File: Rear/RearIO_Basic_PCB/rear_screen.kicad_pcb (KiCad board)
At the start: 2 copper layers, 99.5 x 79.4 mm, 49 parts, among them J1 Conn_01x02_Pin, J13 USB_C_Receptacle_USB2.0, J2 Conn_01x02_Pin, J3 Conn_01x02_Pin, J4 Conn_01x02_Pin, J5 Conn_01x02_Pin, J6 Conn_01x02_Pin, J7 Conn_01x08_Socket, Q1 NTMFS4C03N-HXY, Q2 NTMFS4C03N-HXY, Q3 NTMFS4C03N-HXY, Q4 NTMFS4C03N-HXY, Q6 NTMFS4C03N-HXY, Q7 NTMFS4C03N-HXY, U1 MIC4426, U2 MIC4426, U3 AOZ1280CI

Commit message: wip
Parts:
- moved D4 2.80 mm to (141.2, 129.6)
- moved Q3 2.80 mm to (140.0, 122.5)
- moved Q4 2.80 mm to (130.4, 122.5)
- moved J4 2.80 mm to (137.7, 133.0)
- moved D3 2.10 mm to (115.6, 129.7)
- moved J3 2.10 mm to (112.2, 133.0)
- moved Q6 2.10 mm to (111.2, 121.2)
- moved Q2 1.28 mm to (157.0, 122.9)
- moved D2 1.28 mm to (90.1, 129.6)
- moved D5 1.28 mm to (166.8, 129.7)
- moved J2 1.28 mm to (86.8, 133.0)
- moved J5 1.28 mm to (162.7, 133.1)
- moved Q1 1.28 mm to (170.2, 122.9)
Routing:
- net Net-(Q6-G): track 36.2 -> 37.0 mm
- net Net-(Q1-G): track 66.2 -> 65.7 mm
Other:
- outline, holes or cut-outs redrawn
- board text added: "HP1"
- board text added: "HP2"
- board text added: "INPUT"
- board text added: "LP1"
- board text added: "LP2"
- board text added: "v0.2 09/23"
- board text removed: "v0.1a 08/23"

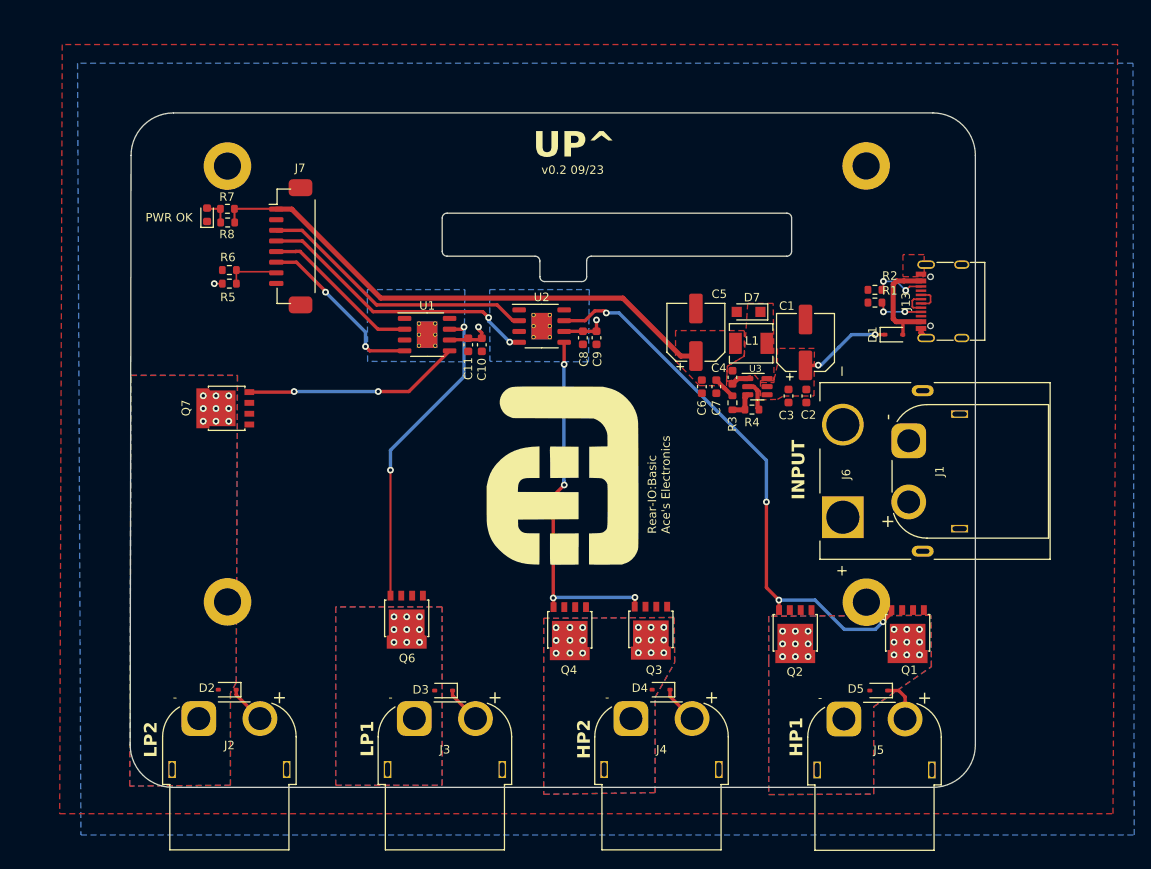
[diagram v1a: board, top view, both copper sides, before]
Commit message: small routing and layout changes, removed USB
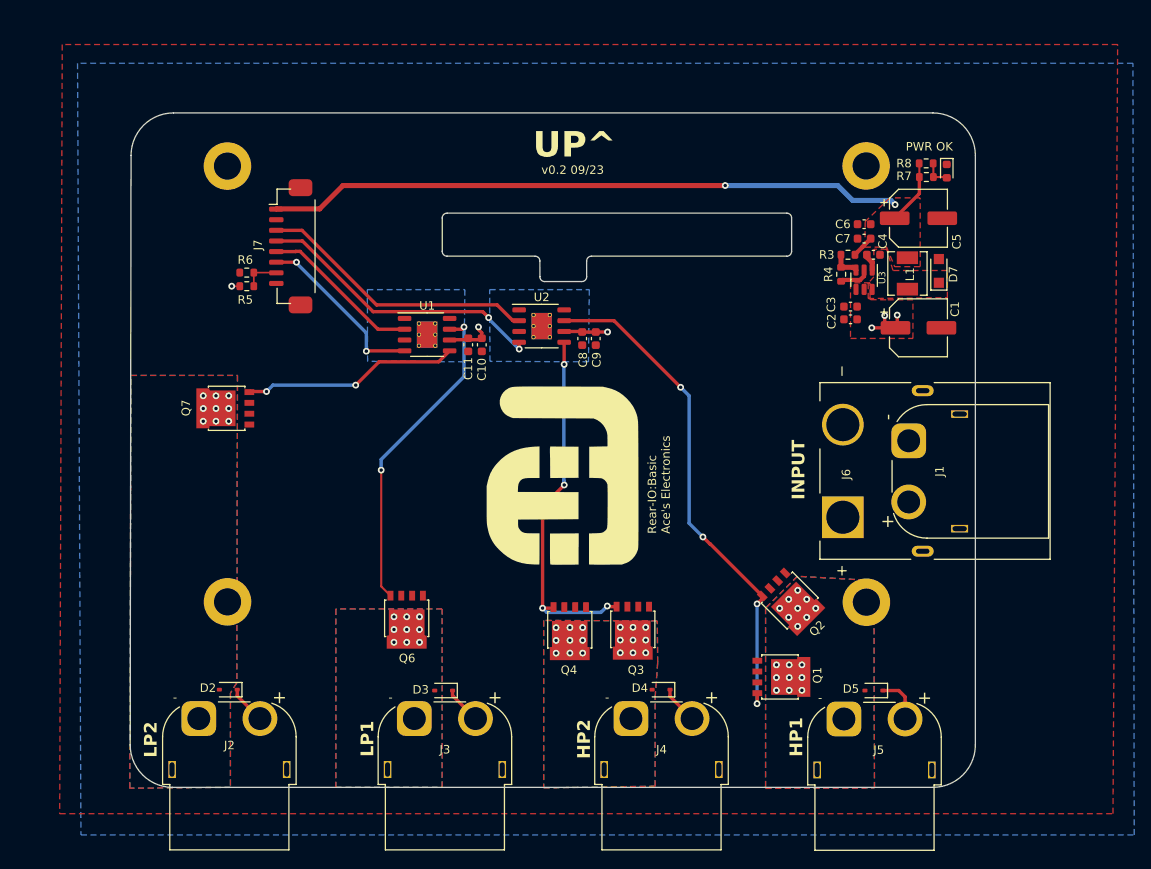
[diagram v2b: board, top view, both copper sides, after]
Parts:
- removed D1: 1N5819WS, Diode_SMD:D_SOD-323
- removed J13: USB_C_Receptacle_USB2.0, Connector_USB:USB_C_Receptacle_G-Switch_GT-USB-7010ASV
- removed R1, R2: 5.1k, Resistor_SMD:R_0603_1608Metric
- moved D6 87.2 mm to (174.8, 68.6), turned to -90 degrees
- moved R8 82.5 mm to (172.4, 67.6), turned to 0 degrees
- moved R7 82.4 mm to (172.4, 69.2), turned to 180 degrees
- moved C5 29.4 mm to (171.5, 74.1), turned to 0 degrees
- moved C6 27.0 mm to (165.1, 74.8), turned to 180 degrees
- moved C7 24.6 mm to (165.1, 76.5), turned to 180 degrees
- moved D7 22.9 mm to (173.9, 80.3), turned to 90 degrees
- moved R3 22.1 mm to (163.2, 78.4), turned to 180 degrees
- moved C4 22.0 mm to (166.2, 78.4), turned to 0 degrees
- moved L1 20.2 mm to (170.2, 80.6), turned to 90 degrees
- moved R4 19.1 mm to (162.4, 80.7), turned to -90 degrees
- moved U3 17.8 mm to (165.1, 81.3), turned to -90 degrees
- moved Q1 15.9 mm to (155.2, 128.1), turned to 0 degrees
- moved C1 13.4 mm to (171.5, 87.0), turned to 0 degrees
- moved C3 12.8 mm to (163.5, 84.5), turned to 180 degrees
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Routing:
- net +5V: track 65.8 -> 85.3 mm, vias 0 -> 2
- net VBUS: track 12.6 -> 0.00 mm
- net Net-(J13-CC2): track 6.14 -> 0.00 mm, vias 2 -> 0
- net Net-(Q1-G): track 65.7 -> 59.7 mm
- net Net-(J13-CC1): track 5.61 -> 0.00 mm, vias 2 -> 0
- net VIN: track 40.8 -> 37.0 mm, vias 5 -> 6
- net USB_D+: track 3.09 -> 0.00 mm
- net USB_D-: track 2.89 -> 0.00 mm
- net GPIO14: track 6.41 -> 4.21 mm
- net GND: track 5.03 -> 3.66 mm
- net GPIO11: track 33.8 -> 34.8 mm
- net Net-(Q6-G): track 37.0 -> 37.9 mm

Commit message: routing and layout changes
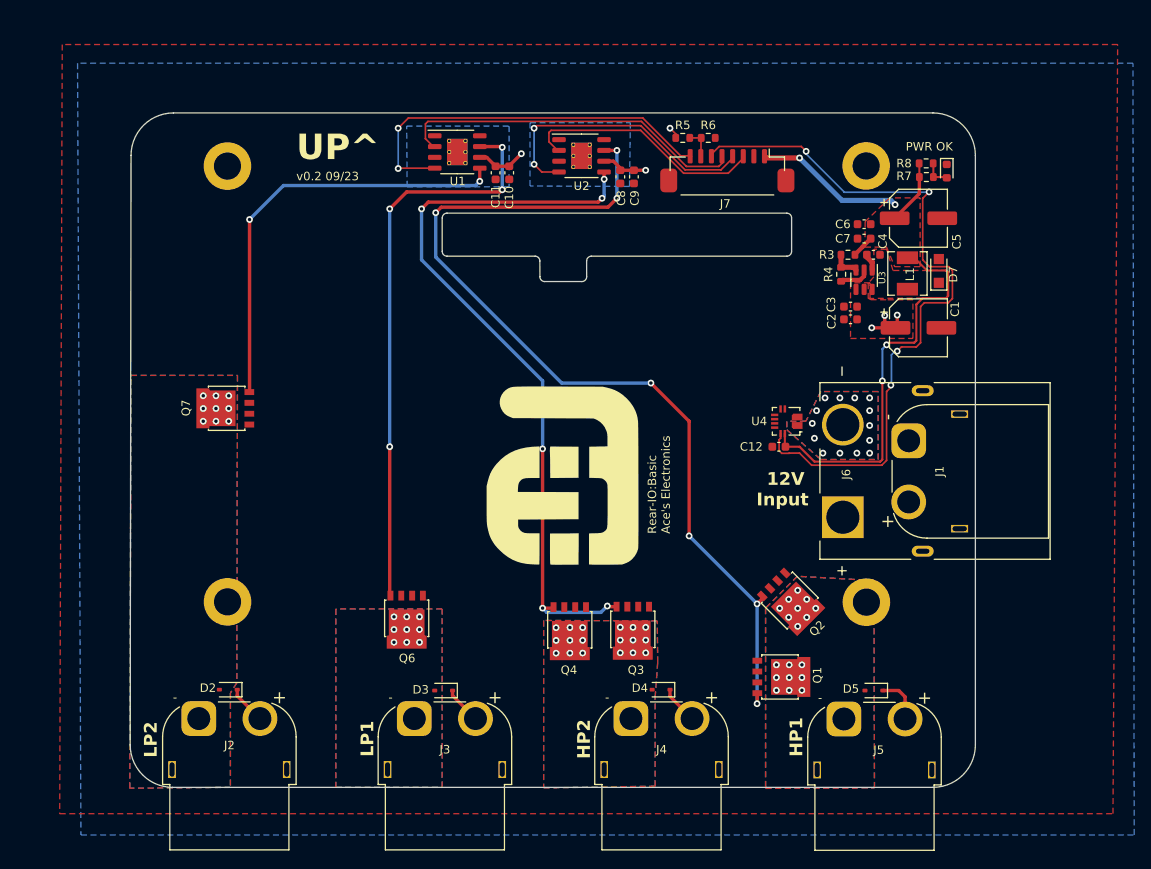
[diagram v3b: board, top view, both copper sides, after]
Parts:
- added C12: 100nF, Capacitor_SMD:C_0603_1608Metric, F.Cu at (155.1, 101.0)
- added U4: ACS711xEXLT-31AB, Sensor_Current:Allegro_QFN-12-10-1EP_3x3mm_P0.5mm, F.Cu at (156.0, 98.0)
- moved R6 56.6 mm to (146.8, 64.6), turned to 0 degrees
- moved R5 54.2 mm to (143.8, 64.6)
- moved J7 51.9 mm to (149.0, 68.8), turned to 180 degrees
- moved U1 21.8 mm to (117.2, 66.3)
- moved U2 20.6 mm to (131.8, 66.8)
- moved C10 20.5 mm to (123.3, 68.8)
- moved C11 20.5 mm to (121.7, 68.8)
- moved C8 19.6 mm to (136.4, 69.2)
- moved C9 19.6 mm to (138.0, 69.2)
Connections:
- J6 pad 1: GND -> BATT-
- U1 pad 4: GPIO13 -> GPIO21
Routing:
- net GPIO13: track 20.8 -> 85.1 mm, vias 2 -> 4
- net Net-(Q1-G): track 59.7 -> 111.2 mm, vias 4 -> 7
- net GPIO21: track 0.00 -> 45.8 mm, vias 0 -> 2
- net Net-(Q3-G): track 43.0 -> 88.7 mm, vias 4 -> 6
- net Net-(Q6-G): track 37.9 -> 67.4 mm, vias 2 -> 4
- net Net-(Q7-G): track 25.6 -> 50.8 mm
- net GPIO12: track 18.9 -> 41.4 mm
- net +5V: track 85.3 -> 76.0 mm, vias 2 -> 4
- net GPIO10: track 33.0 -> 28.7 mm
- net VIN: track 37.0 -> 38.4 mm
- net GPIO14: track 4.21 -> 3.11 mm
- net GPIO11: track 34.8 -> 34.0 mm
- net BATT-: vias 0 -> 14
- added copper zone on B.Cu, net BATT-
- added copper zone on F.Cu, net BATT-
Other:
- board text added: "12V Input"
- board text removed: "INPUT"

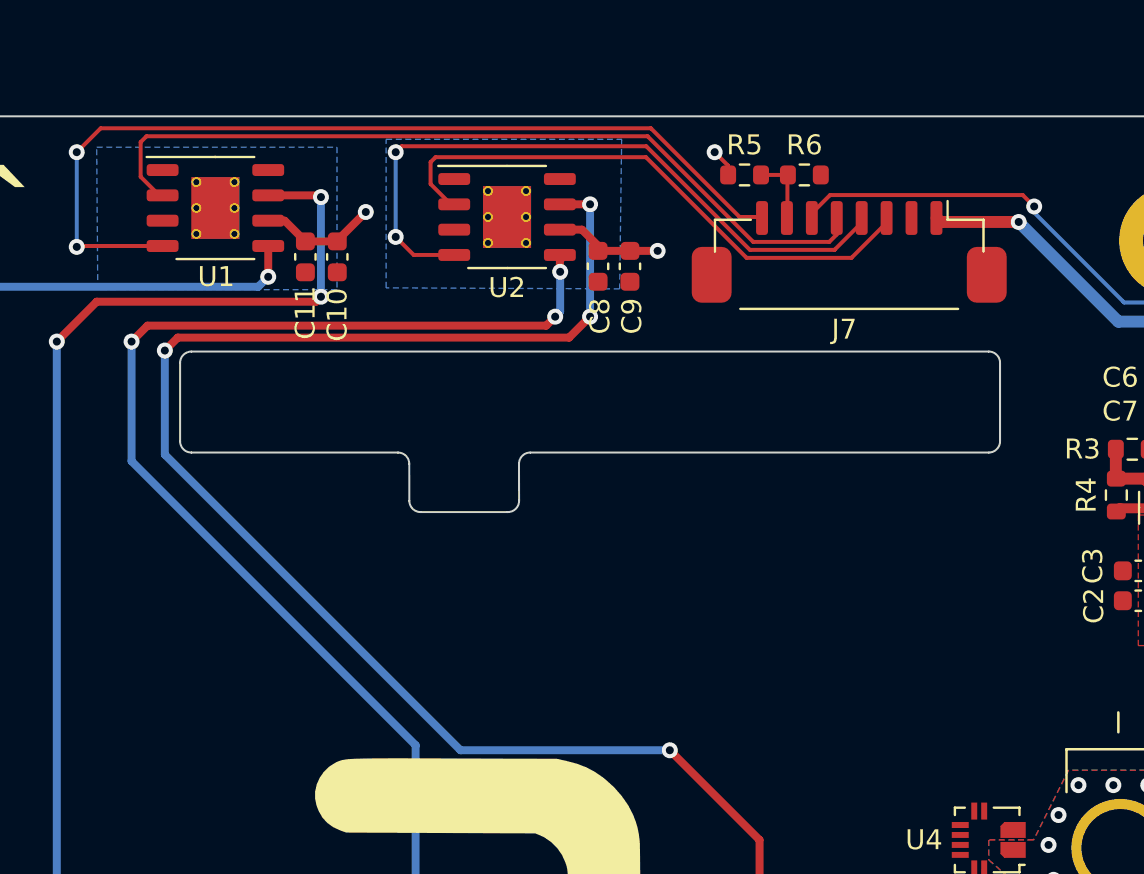
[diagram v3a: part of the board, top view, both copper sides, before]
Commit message: v0.2 submitted to JLCPCB
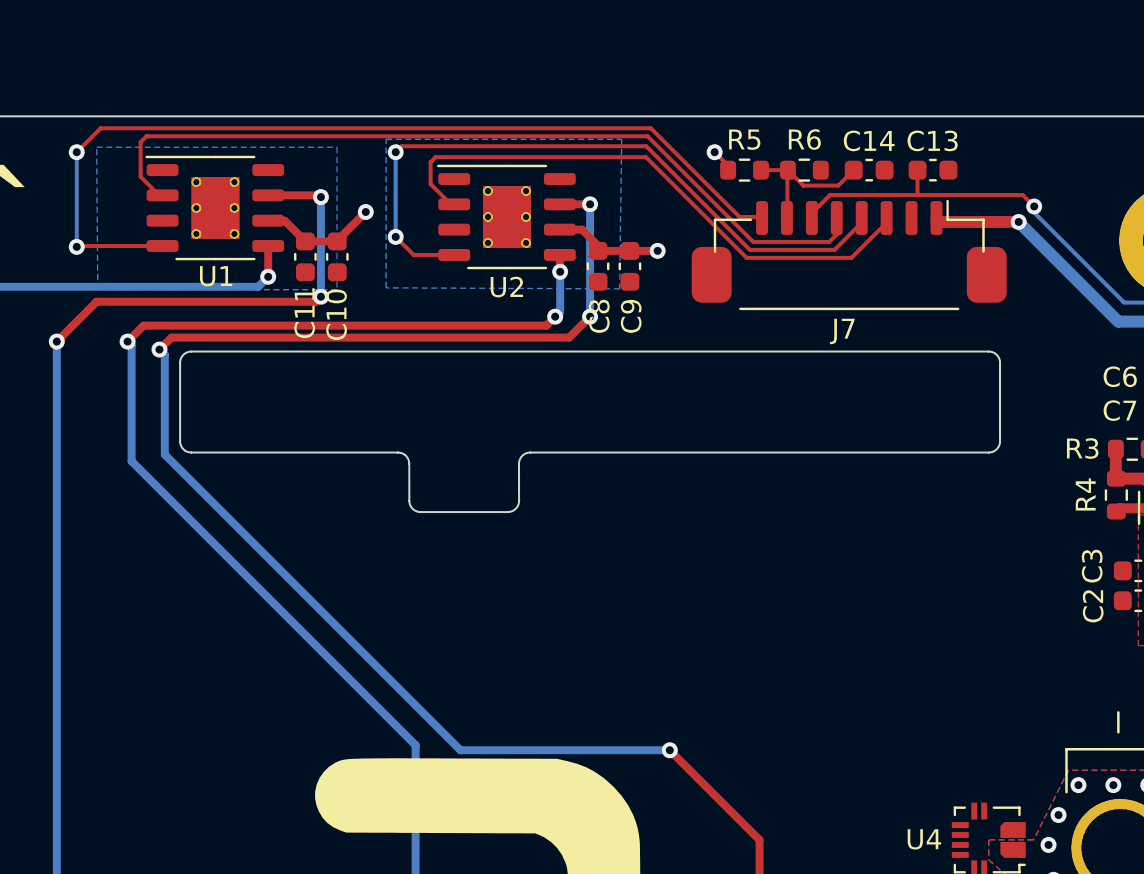
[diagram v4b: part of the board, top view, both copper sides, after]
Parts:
- added C13: 100nF, Capacitor_SMD:C_0603_1608Metric, F.Cu at (153.2, 64.4)
- added C14: 100nF, Capacitor_SMD:C_0603_1608Metric, F.Cu at (150.0, 64.4)
- moved R5 0.24 mm to (143.8, 64.4)
- moved R6 0.24 mm to (146.8, 64.4)
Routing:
- net GPIO14: track 3.11 -> 7.39 mm
- net GPIO13: track 85.1 -> 86.3 mm

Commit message: WIP
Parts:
- removed C10, C8: 10uF, Capacitor_SMD:C_0603_1608Metric
- removed C11, C9: 100nF, Capacitor_SMD:C_0603_1608Metric
- removed R7: 5.1k, Resistor_SMD:R_0603_1608Metric
- removed U1, U2: MIC4426, Package_SO:HSOP-8-1EP_3.9x4.9mm_P1.27mm_EP2.41x3.1mm_ThermalVias
- added D1: CI20S120M3, Package_TO_SOT_SMD:TO-263-2_TabPin1, F.Cu at (152.3, 86.6)
- added D8: CI20S120M3, Package_TO_SOT_SMD:TO-263-2_TabPin1, F.Cu at (151.2, 101.5)
- added Q10: MMBT3904, Package_TO_SOT_SMD:SOT-23, F.Cu at (83.1, 75.7)
- added Q5: MMBT3904, Package_TO_SOT_SMD:SOT-23, F.Cu at (83.1, 89.8)
- added Q8: MMBT3904, Package_TO_SOT_SMD:SOT-23, F.Cu at (83.2, 85.0)
- added Q9: MMBT3904, Package_TO_SOT_SMD:SOT-23, F.Cu at (83.2, 80.4)
- added R1: 1k, Resistor_SMD:R_0603_1608Metric, F.Cu at (86.6, 88.8)
- added R10: 1k, Resistor_SMD:R_0603_1608Metric, F.Cu at (86.8, 79.5)
- added R11: 16k, Resistor_SMD:R_0603_1608Metric, F.Cu at (86.6, 90.5)
- added R12: 1k, Resistor_SMD:R_0603_1608Metric, F.Cu at (86.5, 74.5)
- added R13: 16k, Resistor_SMD:R_0603_1608Metric, F.Cu at (87.0, 81.2)
- added R14: 16k, Resistor_SMD:R_0603_1608Metric, F.Cu at (86.7, 76.2)
- added R2: 16k, Resistor_SMD:R_0603_1608Metric, F.Cu at (86.7, 85.8)
- added R9: 1k, Resistor_SMD:R_0603_1608Metric, F.Cu at (86.7, 84.0)
- moved C1 64.5 mm to (107.0, 84.8)
- moved C2 64.5 mm to (99.0, 83.8)
- moved C3 64.5 mm to (99.0, 82.2)
- moved C5 64.5 mm to (107.0, 71.8)
- moved C7 64.5 mm to (100.6, 74.2)
- moved D7 64.5 mm to (109.5, 78.0)
- moved R4 64.5 mm to (97.9, 78.5)
- moved R8 64.5 mm to (108.0, 65.4)
- moved C4 64.5 mm to (101.8, 76.2)
- moved C6 64.5 mm to (100.7, 72.5)
- moved D6 64.5 mm to (110.4, 66.3)
- moved L1 64.5 mm to (105.8, 78.3)
- moved R3 64.5 mm to (98.7, 76.2)
- moved U3 64.5 mm to (100.7, 79.1)
- moved D5 50.6 mm to (115.7, 129.7)
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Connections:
- C1 pad 1: VIN -> +BATT
- C2 pad 1: VIN -> +BATT
- C3 pad 1: VIN -> +BATT
- D2 pad 1: VIN -> +BATT
- D3 pad 1: VIN -> +BATT
- D4 pad 1: VIN -> +BATT
- D5 pad 1: VIN -> +BATT
- J1 pad 1: GND -> BATT-
- J1 pad 2: VIN -> Net-(D1-A)
- J2 pad 2: VIN -> +BATT
- J3 pad 2: VIN -> +BATT
- J4 pad 2: VIN -> +BATT
- J5 pad 2: VIN -> +BATT
- J6 pad 2: VIN -> Net-(D8-A)
- R5 pad 1: VIN -> +BATT
- U3 pad 4: VIN -> +BATT
- U3 pad 5: VIN -> +BATT
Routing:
- net Net-(Q6-G): track 67.4 -> 156.7 mm, vias 4 -> 2
- net GPIO10: track 28.7 -> 98.1 mm
- net GPIO13: track 86.3 -> 24.7 mm, vias 4 -> 2
- net GPIO11: track 34.0 -> 92.4 mm, vias 2 -> 0
- net Net-(Q3-G): track 89.0 -> 140.9 mm, vias 6 -> 2
- net GPIO12: track 41.4 -> 87.3 mm
- net VIN: track 38.2 -> 0.00 mm, vias 6 -> 0
- net +BATT: track 0.00 -> 32.8 mm, vias 0 -> 77
- net GPIO21: track 45.8 -> 77.2 mm, vias 2 -> 0
- net GND: track 3.66 -> 31.2 mm, vias 0 -> 42
- net +5V: track 76.0 -> 83.9 mm, vias 4 -> 2
- net Net-(Q1-G): track 111.7 -> 107.0 mm, vias 7 -> 4
- net Net-(Q10-C): track 50.8 -> 46.8 mm
- net Net-(Q9-B): track 0.00 -> 1.85 mm
- net Net-(Q8-B): track 0.00 -> 1.75 mm
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- added copper zone on B.Cu, net +BATT
- added copper zone on F.Cu, net +BATT
- added copper zone on B.Cu, net GND
- added copper zone on B.Cu, net Net-(D1-A)
- added copper zone on F.Cu, net Net-(D1-A)
- added copper zone on B.Cu, net Net-(D8-A)
- added copper zone on F.Cu, net Net-(D8-A)
- removed copper zone on B.Cu, net VIN
- removed copper zone on F.Cu, net VIN
- removed copper zone on B.Cu, net unconnected-(U1-TH-Pad9)
- removed copper zone on B.Cu, net unconnected-(U2-TH-Pad9)
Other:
- board size 99.5 x 79.4 mm -> 99.5 x 81.5 mm
- board text added: "Sol."
- board text added: "Veh."
- board text added: "v0.3 12/23"
- board text removed: "12V Input"
- board text removed: "v0.2 09/23"
